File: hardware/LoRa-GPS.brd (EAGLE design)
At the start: 50.8 x 17.8 mm, 34 parts, among them J2 CON-SMA-EDGE-S, J3 USB3085-XX-X_REVD, Q1 IRLML6402, U1 MCP1703-3302E/CB, Y1 CRYSTAL.ABS07

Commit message: bat mon. DRC OK
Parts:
- moved R5 2.92 mm to (38.1, 11.8), turned to 90 degrees
- moved C11 0.38 mm to (35.2, 8.89)
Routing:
- net A4: track 41.4 -> 42.8 mm
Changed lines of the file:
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@@
 <drawing>
 <settings>
-<setting alwaysvectorfont="yes"/>
+<setting alwaysvectorfont="no"/>
 <setting keepoldvectorfont="yes"/>
 <setting verticaltext="up"/>
@@
 <attribute name="MF" value="RF Solutions" x="2.413" y="4.064" size="1.778" layer="27" font="vector" ratio="15" display="off"/>
 <attribute name="MP" value="CON-SMA-EDGE-S" x="2.413" y="4.064" size="1.778" layer="27" font="vector" ratio="15" display="off"/>
+<attribute name="NAME" x="0.413" y="8.064" size="0.8128" layer="25"/>
 <attribute name="NAME" x="0.413" y="8.064" size="0.8128" layer="26"/>
-<attribute name="NAME" x="0.413" y="8.064" size="0.8128" layer="25"/>
 <attribute name="PACKAGE" value="None" x="2.413" y="4.064" size="1.778" layer="27" font="vector" ratio="15" display="off"/>
 <attribute name="PRICE" value="None" x="2.413" y="4.064" size="1.778" layer="27" font="vector" ratio="15" display="off"/>
@@
 <attribute name="VALUE" x="42.545" y="8.255" size="1.27" layer="27" rot="R90"/>
 </element>
-<element name="R5" library="rcl" library_urn="urn:adsk.eagle:library:334" package="R0603" package3d_urn="urn:adsk.eagle:package:23555/3" value="1M" x="38.1" y="8.89" smashed="yes" rot="R270">
-<attribute name="NAME" x="38.735" y="9.525" size="1.27" layer="25" rot="R270"/>
-<attribute name="POPULARITY" value="77" x="38.1" y="8.89" size="1.778" layer="27" font="vector" ratio="15" rot="R270" display="off"/>
-<attribute name="SPICEPREFIX" value="R" x="38.1" y="8.89" size="1.778" layer="27" font="vector" ratio="15" rot="R270" display="off"/>
-<attribute name="VALUE" x="36.195" y="9.525" size="1.27" layer="27" rot="R270"/>
-</element>
-<element name="C11" library="nootropicdesign" package="C0603-THINCREAM" value="100nF" x="35.56" y="8.89" smashed="yes" rot="R270">
-<attribute name="MF" value="AVX" x="35.56" y="8.89" size="1.778" layer="27" font="vector" ratio="15" rot="R270" display="off"/>
-<attribute name="MPN" value="02016D104KAT2A" x="35.56" y="8.89" size="1.778" layer="27" font="vector" ratio="15" rot="R270" display="off"/>
-<attribute name="NAME" x="36.322" y="9.779" size="1.27" layer="25" rot="R270"/>
-<attribute name="OC_FARNELL" value="1657913" x="35.56" y="8.89" size="1.778" layer="27" font="vector" ratio="15" rot="R270" display="off"/>
-<attribute name="VALUE" x="33.528" y="9.779" size="1.27" layer="27" rot="R270"/>
+<element name="R5" library="rcl" library_urn="urn:adsk.eagle:library:334" package="R0603" package3d_urn="urn:adsk.eagle:package:23555/3" value="1M" x="38.1" y="11.811" smashed="yes" rot="R90">
+<attribute name="NAME" x="37.465" y="11.176" size="1.27" layer="25" rot="R90"/>
+<attribute name="POPULARITY" value="77" x="38.1" y="11.811" size="1.778" layer="27" font="vector" ratio="15" rot="R90" display="off"/>
+<attribute name="SPICEPREFIX" value="R" x="38.1" y="11.811" size="1.778" layer="27" font="vector" ratio="15" rot="R90" display="off"/>
+<attribute name="VALUE" x="40.005" y="11.176" size="1.27" layer="27" rot="R90"/>
+</element>
+<element name="C11" library="nootropicdesign" package="C0603-THINCREAM" value="100nF" x="35.179" y="8.89" smashed="yes" rot="R270">
+<attribute name="MF" value="AVX" x="35.179" y="8.89" size="1.778" layer="27" font="vector" ratio="15" rot="R270" display="off"/>
+<attribute name="MPN" value="02016D104KAT2A" x="35.179" y="8.89" size="1.778" layer="27" font="vector" ratio="15" rot="R270" display="off"/>
+<attribute name="NAME" x="35.941" y="9.779" size="1.27" layer="25" rot="R270"/>
+<attribute name="OC_FARNELL" value="1657913" x="35.179" y="8.89" size="1.778" layer="27" font="vector" ratio="15" rot="R270" display="off"/>
+<attribute name="VALUE" x="33.147" y="9.779" size="1.27" layer="27" rot="R270"/>
 </element>
 </elements>
@@
 <vertex x="50.8" y="17.78"/>
 </polygon>
-<wire x1="22.225" y1="11.557" x2="22.16126875" y2="11.435584375" width="0.1524" layer="1"/>
 <via x="13.97" y="3.81" extent="1-16" drill="0.254"/>
 <contactref element="J2" pad="G1"/>
@@
 <contactref element="R5" pad="1"/>
 <contactref element="C11" pad="1"/>
-<wire x1="40.64" y1="9.74" x2="38.1" y2="9.74" width="0.1524" layer="1"/>
-<wire x1="38.1" y1="9.74" x2="35.5718" y2="9.74" width="0.1524" layer="1"/>
-<wire x1="35.5718" y1="9.74" x2="35.56" y2="9.7282" width="0.254" layer="1"/>
+<wire x1="39.37" y1="11.01" x2="38.244721875" y2="11.01" width="0.1524" layer="1"/>
+<wire x1="38.244721875" y1="11.01" x2="38.1" y2="10.961" width="0.1524" layer="1"/>
+<wire x1="35.1908" y1="9.74" x2="35.179" y2="9.7282" width="0.254" layer="1"/>
 <wire x1="17.4244" y1="11.9126" x2="16.5354" y2="11.9126" width="0.1524" layer="1"/>
 <wire x1="19.9136" y1="14.4018" x2="17.4244" y2="11.9126" width="0.1524" layer="1"/>
@@
 <wire x1="16.5354" y1="11.9126" x2="16.5044125" y2="12.00126875" width="0.1524" layer="1"/>
 <wire x1="40.7162" y1="9.779" x2="40.64" y2="9.74" width="0.1524" layer="1"/>
+<wire x1="38.1" y1="10.961" x2="36.4118" y2="10.961" width="0.1524" layer="1"/>
+<wire x1="36.4118" y1="10.961" x2="35.1908" y2="9.74" width="0.1524" layer="1"/>
+<wire x1="40.64" y1="9.74" x2="39.37" y2="11.01" width="0.1524" layer="1"/>
 </signal>
 </signals>

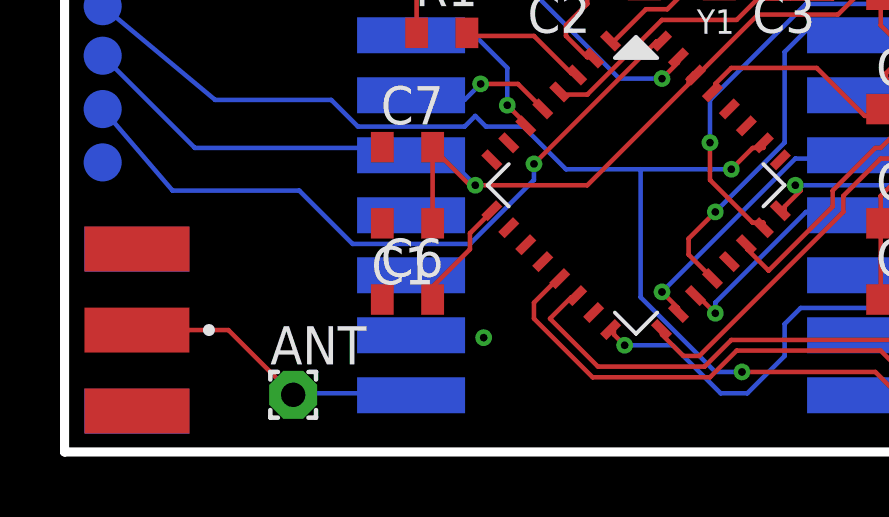
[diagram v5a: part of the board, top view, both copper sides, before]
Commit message: add FB for VDDANA
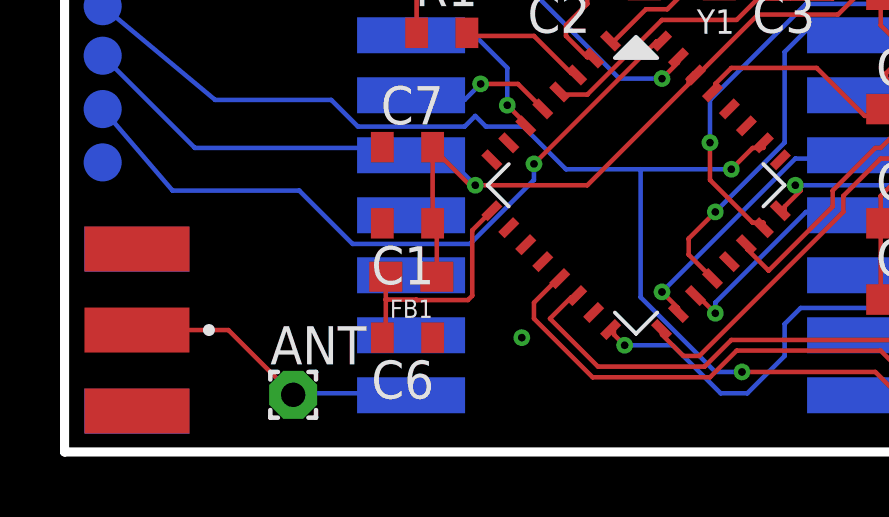
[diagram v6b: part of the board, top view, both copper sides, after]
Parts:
- added FB1: 30Ω/1.8A, SparkFun-Coils:0603
- moved C6 1.27 mm to (11.4, 3.81), turned to 180 degrees
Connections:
- net N$1: now also FB1.2
- net VCC: now also FB1.1
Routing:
- net N$1: track 3.78 -> 8.13 mm
- net VCC: track 55.5 -> 57.4 mm
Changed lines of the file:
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@@
 <drawing>
 <settings>
-<setting alwaysvectorfont="no"/>
+<setting alwaysvectorfont="yes"/>
 <setting keepoldvectorfont="yes"/>
 <setting verticaltext="up"/>
@@
 <layer number="37" name="tTest" color="7" fill="1" visible="no" active="yes"/>
 <layer number="38" name="bTest" color="7" fill="1" visible="no" active="yes"/>
-<layer number="39" name="tKeepout" color="4" fill="11" visible="yes" active="yes"/>
+<layer number="39" name="tKeepout" color="4" fill="11" visible="no" active="yes"/>
 <layer number="40" name="bKeepout" color="1" fill="11" visible="no" active="yes"/>
 <layer number="41" name="tRestrict" color="4" fill="10" visible="no" active="yes"/>
@@
 <attribute name="VALUE" x="27.051" y="13.208" size="1.27" layer="27"/>
 </element>
-<element name="C6" library="nootropicdesign" package="C0603-THINCREAM" value="100nF" x="11.43" y="5.08" smashed="yes">
-<attribute name="MF" value="AVX" x="11.43" y="5.08" size="1.778" layer="27" display="off"/>
-<attribute name="MPN" value="02016D104KAT2A" x="11.43" y="5.08" size="1.778" layer="27" display="off"/>
-<attribute name="NAME" x="10.541" y="5.842" size="1.27" layer="25"/>
-<attribute name="OC_FARNELL" value="1657913" x="11.43" y="5.08" size="1.778" layer="27" display="off"/>
-<attribute name="VALUE" x="10.541" y="3.048" size="1.27" layer="27"/>
+<element name="C6" library="nootropicdesign" package="C0603-THINCREAM" value="100nF" x="11.43" y="3.81" smashed="yes" rot="R180">
+<attribute name="MF" value="AVX" x="11.43" y="3.81" size="1.778" layer="27" rot="R180" display="off"/>
+<attribute name="MPN" value="02016D104KAT2A" x="11.43" y="3.81" size="1.778" layer="27" rot="R180" display="off"/>
+<attribute name="NAME" x="12.319" y="3.048" size="1.27" layer="25" rot="R180"/>
+<attribute name="OC_FARNELL" value="1657913" x="11.43" y="3.81" size="1.778" layer="27" rot="R180" display="off"/>
+<attribute name="VALUE" x="12.319" y="5.842" size="1.27" layer="27" rot="R180"/>
 </element>
 <element name="C7" library="nootropicdesign" package="C0603-THINCREAM" value="100nF" x="11.43" y="10.16" smashed="yes">
@@
 <attribute name="OC_FARNELL" value="1657913" x="35.179" y="8.89" size="1.778" layer="27" font="vector" ratio="15" rot="R270" display="off"/>
 <attribute name="VALUE" x="33.147" y="9.779" size="1.27" layer="27" rot="R270"/>
+</element>
+<element name="FB1" library="SparkFun-Coils" library_urn="urn:adsk.eagle:library:512" package="0603" package3d_urn="urn:adsk.eagle:package:37574/1" value="30Ω/1.8A" x="11.557" y="5.842" smashed="yes" rot="R180">
+<attribute name="NAME" x="11.557" y="5.08" size="0.6096" layer="25" font="vector" ratio="20" rot="R180" align="bottom-center"/>
+<attribute name="PROD_ID" value="NDUC-07859" x="11.557" y="5.842" size="1.778" layer="27" font="vector" ratio="15" rot="R180" display="off"/>
+<attribute name="VALUE" x="11.557" y="6.604" size="0.6096" layer="27" font="vector" ratio="20" rot="R180" align="top-center"/>
 </element>
 </elements>
@@
 <contactref element="RADIO" pad="A8"/>
 <contactref element="RADIO" pad="A1"/>
-<contactref element="SAMD21" pad="10"/>
 <contactref element="GPS" pad="3"/>
 <contactref element="C8" pad="2"/>
@@
 <vertex x="50.8" y="17.78"/>
 </polygon>
-<via x="13.97" y="3.81" extent="1-16" drill="0.254"/>
+<via x="15.24" y="3.81" extent="1-16" drill="0.254"/>
 <contactref element="J2" pad="G1"/>
 <contactref element="J2" pad="G3"/>
@@
 <via x="42.164" y="15.113" extent="1-16" drill="0.254"/>
 <via x="24.13" y="16.891" extent="1-16" drill="0.254"/>
+<contactref element="SAMD21" pad="10"/>
 </signal>
 <signal name="VCC">
@@
 <wire x1="13.5128" y1="8.89" x2="12.6238" y2="9.779" width="0.1524" layer="1"/>
 <wire x1="13.6906" y1="8.89" x2="13.5128" y2="8.89" width="0.1524" layer="1"/>
+<contactref element="FB1" pad="1"/>
+<wire x1="12.2682" y1="7.62" x2="12.407" y2="7.4812" width="0.1524" layer="1"/>
+<wire x1="12.407" y1="7.4812" x2="12.407" y2="5.842" width="0.1524" layer="1"/>
 </signal>
 <signal name="VIN">
@@
 <contactref element="C6" pad="2"/>
 <contactref element="SAMD21" pad="9"/>
-<wire x1="13.5128" y1="7.2898" x2="14.224" y2="8.001" width="0.1524" layer="1"/>
-<wire x1="13.5128" y1="6.7564" x2="13.5128" y2="7.2898" width="0.1524" layer="1"/>
-<wire x1="12.2682" y1="5.5118" x2="13.5128" y2="6.7564" width="0.1524" layer="1"/>
-<wire x1="12.2682" y1="5.08" x2="12.2682" y2="5.5118" width="0.1524" layer="1"/>
-<wire x1="14.224" y1="8.001" x2="14.241671875" y2="8.04146875" width="0.1524" layer="1"/>
+<contactref element="FB1" pad="2"/>
+<wire x1="10.707" y1="5.842" x2="10.707" y2="5.08" width="0.1524" layer="1"/>
+<wire x1="10.707" y1="5.08" x2="10.707" y2="3.9252" width="0.1524" layer="1"/>
+<wire x1="10.707" y1="3.9252" x2="10.5918" y2="3.81" width="0.1524" layer="1"/>
+<wire x1="14.241671875" y1="8.04146875" x2="13.589" y2="7.388796875" width="0.1524" layer="1"/>
+<wire x1="13.589" y1="7.388796875" x2="13.589" y2="5.207" width="0.1524" layer="1"/>
+<wire x1="11.74126875" y1="5.0626" x2="11.72386875" y2="5.08" width="0.1524" layer="1"/>
+<wire x1="11.72386875" y1="5.08" x2="10.707" y2="5.08" width="0.1524" layer="1"/>
+<wire x1="13.589" y1="5.207" x2="13.4446" y2="5.0626" width="0.1524" layer="1"/>
+<wire x1="13.4446" y1="5.0626" x2="11.74126875" y2="5.0626" width="0.1524" layer="1"/>
 </signal>
 <signal name="MOSI">

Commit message: bat mon. more pour. gerber gen
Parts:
- moved TP1 5.68 mm to (6.35, 7.11)
- moved TP5 5.52 mm to (6.35, 9.27)
- moved TP2 5.24 mm to (6.35, 11.9)
- moved TP3 5.11 mm to (6.35, 14.4)
- moved TP4 5.08 mm to (6.35, 16.4)
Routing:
- net SWDIO: track 23.7 -> 17.7 mm
- net VCC: track 57.4 -> 51.8 mm
- net RESET: track 53.4 -> 48.3 mm
- net SWCLK: track 21.7 -> 16.7 mm
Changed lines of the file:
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@@
 <drawing>
 <settings>
-<setting alwaysvectorfont="yes"/>
+<setting alwaysvectorfont="no"/>
 <setting keepoldvectorfont="yes"/>
 <setting verticaltext="up"/>
@@
 <attribute name="VALUE" x="27.051" y="3.048" size="1.27" layer="27"/>
 </element>
-<element name="TP5" library="SparkFun-Passives" package="PAD.03X.05" value="" x="1.27" y="11.43" smashed="yes" rot="MR0">
-<attribute name="MF" value="" x="1.27" y="11.43" size="1.778" layer="28" rot="MR0" display="off"/>
-<attribute name="MPN" value="" x="1.27" y="11.43" size="1.778" layer="28" rot="MR0" display="off"/>
-<attribute name="OC_FARNELL" value="unknown" x="1.27" y="11.43" size="1.778" layer="28" rot="MR0" display="off"/>
-</element>
-<element name="TP4" library="SparkFun-Passives" package="PAD.03X.05" value="" x="1.27" y="16.51" smashed="yes" rot="MR0">
-<attribute name="MF" value="" x="1.27" y="16.51" size="1.778" layer="28" rot="MR0" display="off"/>
-<attribute name="MPN" value="" x="1.27" y="16.51" size="1.778" layer="28" rot="MR0" display="off"/>
-<attribute name="OC_FARNELL" value="unknown" x="1.27" y="16.51" size="1.778" layer="28" rot="MR0" display="off"/>
-</element>
-<element name="TP3" library="SparkFun-Passives" package="PAD.03X.05" value="" x="1.27" y="14.859" smashed="yes" rot="MR0">
-<attribute name="MF" value="" x="1.27" y="14.859" size="1.778" layer="28" rot="MR0" display="off"/>
-<attribute name="MPN" value="" x="1.27" y="14.859" size="1.778" layer="28" rot="MR0" display="off"/>
-<attribute name="OC_FARNELL" value="unknown" x="1.27" y="14.859" size="1.778" layer="28" rot="MR0" display="off"/>
-</element>
-<element name="TP2" library="SparkFun-Passives" package="PAD.03X.05" value="VCC" x="1.27" y="13.208" smashed="yes" rot="MR0">
-<attribute name="MF" value="" x="1.27" y="13.208" size="1.778" layer="28" rot="MR0" display="off"/>
-<attribute name="MPN" value="" x="1.27" y="13.208" size="1.778" layer="28" rot="MR0" display="off"/>
-<attribute name="OC_FARNELL" value="unknown" x="1.27" y="13.208" size="1.778" layer="28" rot="MR0" display="off"/>
+<element name="TP5" library="SparkFun-Passives" package="PAD.03X.05" value="" x="6.35" y="9.271" smashed="yes" rot="MR0">
+<attribute name="MF" value="" x="6.35" y="9.271" size="1.778" layer="28" rot="MR0" display="off"/>
+<attribute name="MPN" value="" x="6.35" y="9.271" size="1.778" layer="28" rot="MR0" display="off"/>
+<attribute name="OC_FARNELL" value="unknown" x="6.35" y="9.271" size="1.778" layer="28" rot="MR0" display="off"/>
+</element>
+<element name="TP4" library="SparkFun-Passives" package="PAD.03X.05" value="" x="6.35" y="16.383" smashed="yes" rot="MR0">
+<attribute name="MF" value="" x="6.35" y="16.383" size="1.778" layer="28" rot="MR0" display="off"/>
+<attribute name="MPN" value="" x="6.35" y="16.383" size="1.778" layer="28" rot="MR0" display="off"/>
+<attribute name="OC_FARNELL" value="unknown" x="6.35" y="16.383" size="1.778" layer="28" rot="MR0" display="off"/>
+</element>
+<element name="TP3" library="SparkFun-Passives" package="PAD.03X.05" value="" x="6.35" y="14.351" smashed="yes" rot="MR0">
+<attribute name="MF" value="" x="6.35" y="14.351" size="1.778" layer="28" rot="MR0" display="off"/>
+<attribute name="MPN" value="" x="6.35" y="14.351" size="1.778" layer="28" rot="MR0" display="off"/>
+<attribute name="OC_FARNELL" value="unknown" x="6.35" y="14.351" size="1.778" layer="28" rot="MR0" display="off"/>
+</element>
+<element name="TP2" library="SparkFun-Passives" package="PAD.03X.05" value="VCC" x="6.35" y="11.938" smashed="yes" rot="MR0">
+<attribute name="MF" value="" x="6.35" y="11.938" size="1.778" layer="28" rot="MR0" display="off"/>
+<attribute name="MPN" value="" x="6.35" y="11.938" size="1.778" layer="28" rot="MR0" display="off"/>
+<attribute name="OC_FARNELL" value="unknown" x="6.35" y="11.938" size="1.778" layer="28" rot="MR0" display="off"/>
 </element>
 <element name="JP1" library="nootropicdesign" package="1X01_LONG" value="M01LONG" x="48.895" y="16.002" smashed="yes" rot="R90">
@@
 <attribute name="OC_FARNELL" value="unknown" x="48.895" y="1.905" size="1.778" layer="27" rot="R90" display="off"/>
 </element>
-<element name="TP1" library="SparkFun-Passives" package="PAD.03X.05" value="GND" x="1.27" y="9.652" smashed="yes" rot="MR180">
-<attribute name="MF" value="" x="1.27" y="9.652" size="1.778" layer="28" rot="MR180" display="off"/>
-<attribute name="MPN" value="" x="1.27" y="9.652" size="1.778" layer="28" rot="MR180" display="off"/>
-<attribute name="OC_FARNELL" value="unknown" x="1.27" y="9.652" size="1.778" layer="28" rot="MR180" display="off"/>
+<element name="TP1" library="SparkFun-Passives" package="PAD.03X.05" value="GND" x="6.35" y="7.112" smashed="yes" rot="MR180">
+<attribute name="MF" value="" x="6.35" y="7.112" size="1.778" layer="28" rot="MR180" display="off"/>
+<attribute name="MPN" value="" x="6.35" y="7.112" size="1.778" layer="28" rot="MR180" display="off"/>
+<attribute name="OC_FARNELL" value="unknown" x="6.35" y="7.112" size="1.778" layer="28" rot="MR180" display="off"/>
 </element>
 <element name="Q1" library="ianc" package="SOT23-3" package3d_urn="urn:adsk.eagle:package:38446/1" value="IRLML6402" x="35.56" y="15.24" smashed="yes" rot="R90">
@@
 <attribute name="MF" value="RF Solutions" x="2.413" y="4.064" size="1.778" layer="27" font="vector" ratio="15" display="off"/>
 <attribute name="MP" value="CON-SMA-EDGE-S" x="2.413" y="4.064" size="1.778" layer="27" font="vector" ratio="15" display="off"/>
+<attribute name="NAME" x="0.413" y="8.064" size="0.8128" layer="26"/>
 <attribute name="NAME" x="0.413" y="8.064" size="0.8128" layer="25"/>
-<attribute name="NAME" x="0.413" y="8.064" size="0.8128" layer="26"/>
 <attribute name="PACKAGE" value="None" x="2.413" y="4.064" size="1.778" layer="27" font="vector" ratio="15" display="off"/>
 <attribute name="PRICE" value="None" x="2.413" y="4.064" size="1.778" layer="27" font="vector" ratio="15" display="off"/>
@@
 <via x="24.13" y="16.891" extent="1-16" drill="0.254"/>
 <contactref element="SAMD21" pad="10"/>
+<via x="18.415" y="11.176" extent="1-16" drill="0.254"/>
+<via x="33.02" y="11.43" extent="1-16" drill="0.254"/>
 </signal>
 <signal name="VCC">
@@
 <contactref element="GPS" pad="5"/>
 <wire x1="11.3792" y1="9.9568" x2="11.2014" y2="10.1346" width="0.1524" layer="16"/>
-<wire x1="1.27" y1="13.208" x2="4.3434" y2="10.1346" width="0.1524" layer="16"/>
-<wire x1="11.2014" y1="10.1346" x2="4.3434" y2="10.1346" width="0.1524" layer="16"/>
+<wire x1="6.35" y1="11.938" x2="8.1534" y2="10.1346" width="0.1524" layer="16"/>
+<wire x1="11.2014" y1="10.1346" x2="8.1534" y2="10.1346" width="0.1524" layer="16"/>
 <wire x1="11.3792" y1="9.9568" x2="11.55" y2="9.89" width="0.1524" layer="16"/>
 <wire x1="38.0238" y1="16.1798" x2="36.6014" y2="16.1798" width="0.1524" layer="1"/>
@@
 <wire x1="19.7358" y1="13.6906" x2="19.898528125" y2="13.698325" width="0.1524" layer="1"/>
 <via x="15.6464" y="9.6012" extent="1-16" drill="0.254"/>
-<wire x1="7.8232" y1="8.7122" x2="3.59954375" y2="8.7122" width="0.1524" layer="16"/>
+<wire x1="7.8232" y1="8.7122" x2="6.828971875" y2="8.7122" width="0.1524" layer="16"/>
 <wire x1="9.6012" y1="6.9342" x2="7.8232" y2="8.7122" width="0.1524" layer="16"/>
 <wire x1="13.5128" y1="6.9342" x2="9.6012" y2="6.9342" width="0.1524" layer="16"/>
 <wire x1="15.6464" y1="9.0678" x2="13.5128" y2="6.9342" width="0.1524" layer="16"/>
 <wire x1="15.6464" y1="9.6012" x2="15.6464" y2="9.0678" width="0.1524" layer="16"/>
-<wire x1="3.59954375" y1="8.7122" x2="1.27" y2="11.43" width="0.1524" layer="16"/>
+<wire x1="6.828971875" y1="8.7122" x2="6.35" y2="9.271" width="0.1524" layer="16"/>
 </signal>
 <signal name="SWCLK">
@@
 <wire x1="20.447" y1="12.9794" x2="20.4642125" y2="13.132640625" width="0.1524" layer="1"/>
 <via x="19.9136" y="12.446" extent="1-16" drill="0.254"/>
-<wire x1="7.4168" y1="16.51" x2="7.9756" y2="17.0688" width="0.1524" layer="16"/>
-<wire x1="1.27" y1="16.51" x2="7.4168" y2="16.51" width="0.1524" layer="16"/>
+<wire x1="7.2898" y1="16.383" x2="7.9756" y2="17.0688" width="0.1524" layer="16"/>
+<wire x1="6.35" y1="16.383" x2="7.2898" y2="16.383" width="0.1524" layer="16"/>
 </signal>
 <signal name="RESET">
@@
 <wire x1="13.335" y1="10.8458" x2="13.6906" y2="11.2014" width="0.1524" layer="16"/>
 <wire x1="9.779" y1="10.8458" x2="13.335" y2="10.8458" width="0.1524" layer="16"/>
-<wire x1="8.89" y1="11.7348" x2="9.779" y2="10.8458" width="0.1524" layer="16"/>
-<wire x1="5.019040625" y1="11.7348" x2="8.89" y2="11.7348" width="0.1524" layer="16"/>
 <wire x1="23.2918" y1="10.1346" x2="23.292640625" y2="10.3042125" width="0.1524" layer="1"/>
-<wire x1="5.019040625" y1="11.7348" x2="1.27" y2="14.859" width="0.1524" layer="16"/>
+<wire x1="6.35" y1="14.351" x2="6.35" y2="14.2748" width="0.1524" layer="16"/>
+<wire x1="9.779" y1="10.8458" x2="6.35" y2="14.2748" width="0.1524" layer="16"/>
 <wire x1="27.0256" y1="2.667" x2="28.8036" y2="0.889" width="0.1524" layer="1"/>
 <wire x1="22.5806" y1="2.667" x2="27.0256" y2="2.667" width="0.1524" layer="1"/>
